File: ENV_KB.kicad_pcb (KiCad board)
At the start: 2 copper layers, 355.7 x 131.8 mm, 177 parts, among them U1 PICO_RP2040

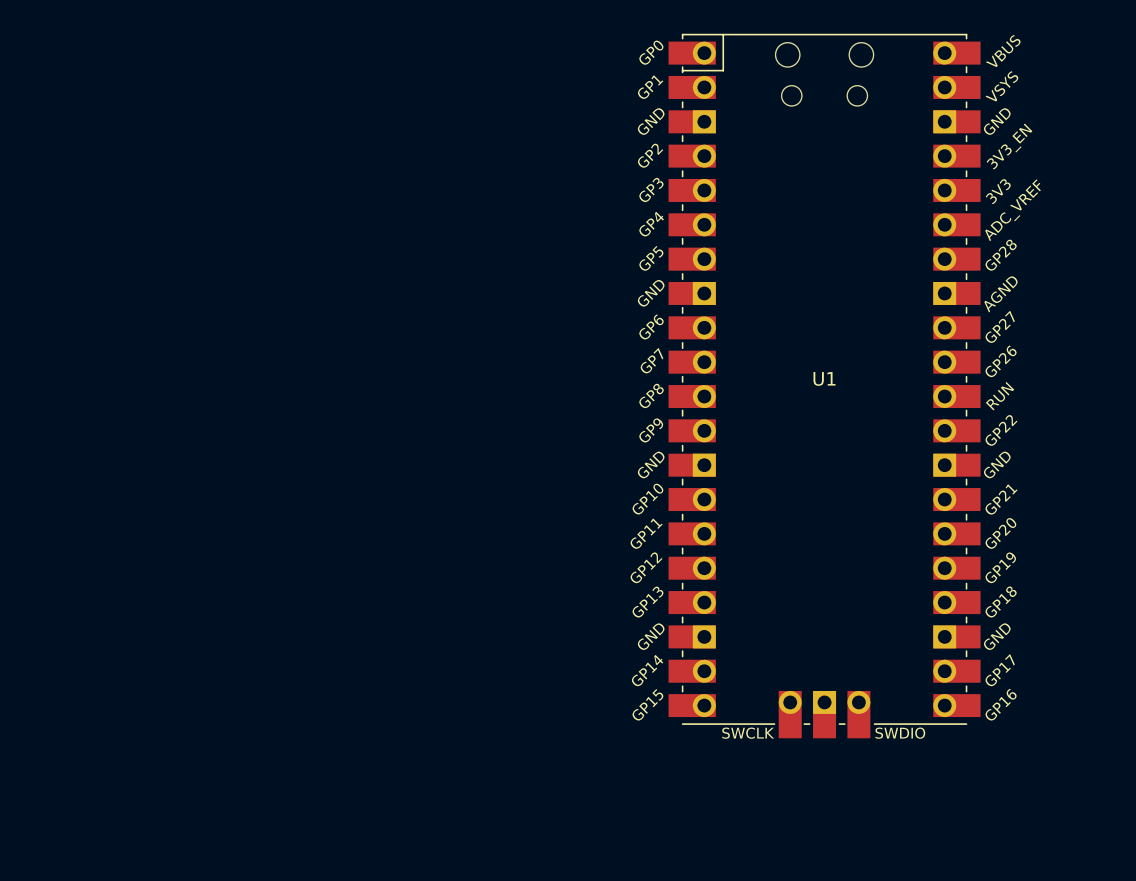
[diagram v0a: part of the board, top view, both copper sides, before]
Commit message: Updated Ratsnest
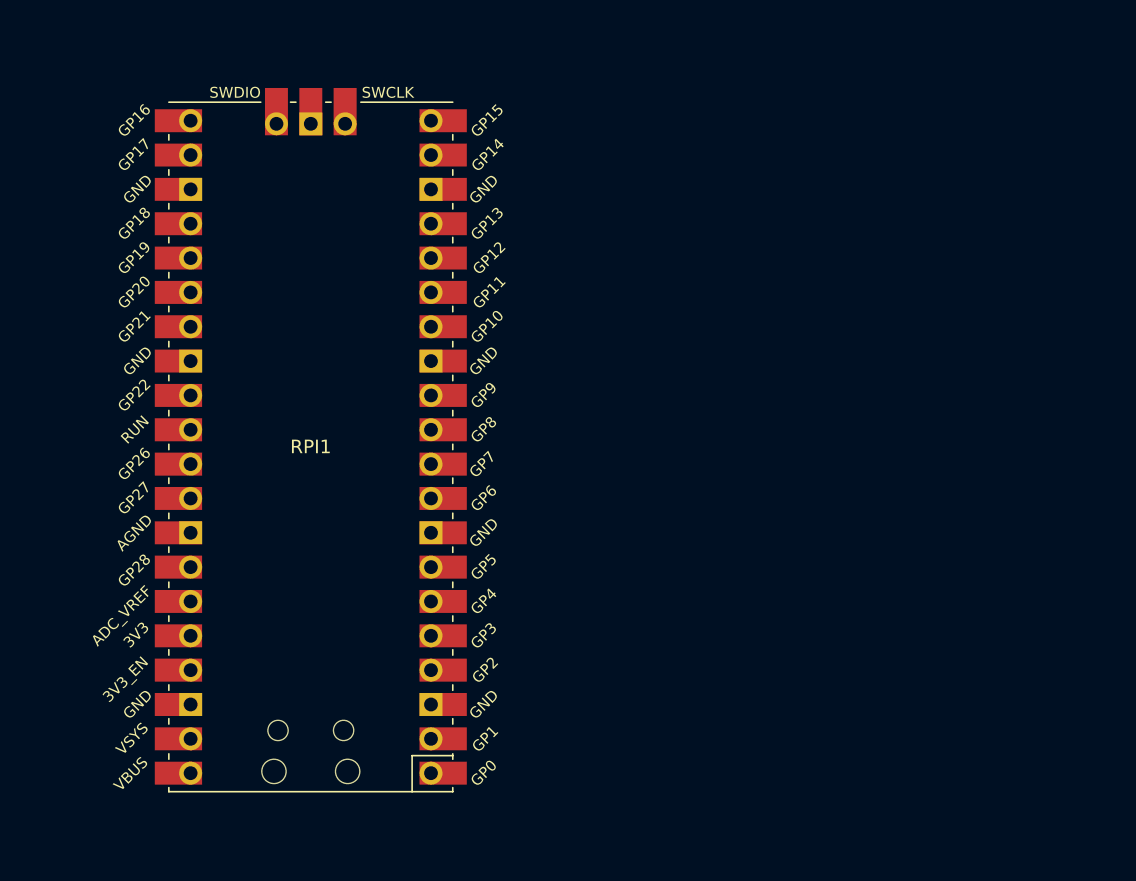
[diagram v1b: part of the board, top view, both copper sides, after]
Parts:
- removed U1: PICO_RP2040, MCU_RaspberryPi_and_Boards.pretty:RPi_Pico_SMD_TH
- added RPI1: Pico, MCU_RaspberryPi_and_Boards.pretty:RPi_Pico_SMD_TH, F.Cu at (198.0, -25.0)

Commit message: Generic Progress
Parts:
- removed RPI1: Pico, MCU_RaspberryPi_and_Boards.pretty:RPi_Pico_SMD_TH
- D_0, D_1, D_10, D_11, D_12, D_13, D_14, D_15, D_16, D_17, D_18, D_19, D_2, D_20, D_21, D_22, D_23, D_24, D_25, D_26, D_27, D_28, D_29, D_3, D_30, D_31, D_32, D_33, D_34, D_35, D_36, D_37, D_38, D_39, D_4, D_40, D_41, D_42, D_43, D_44, D_45, D_46, D_47, D_48, D_49, D_5, D_50, D_51, D_52, D_53, D_54, D_55, D_56, D_57, D_58, D_59, D_6, D_60, D_61, D_62, D_63, D_64, D_65, D_66, D_67, D_68, D_69, D_7, D_70, D_71, D_72, D_73, D_74, D_75, D_76, D_77, D_78, D_79, D_8, D_80, D_81, D_82, D_83, D_84, D_85, D_86, D_87, D_9: moved to F.Cu
- moved K_46 169.3 mm to (408.8, 204.7)
- moved K_11 169.3 mm to (392.2, 147.5)
- moved K_12 169.3 mm to (411.2, 147.5)
- moved K_13 169.3 mm to (435.0, 147.5)
- moved K_19 169.3 mm to (201.7, 176.1)
- moved K_2 169.3 mm to (201.7, 147.5)
- moved K_25 169.3 mm to (316.0, 176.1)
- moved K_30 169.3 mm to (435.0, 176.1)
- moved K_39 169.3 mm to (268.4, 195.2)
- moved K_44 169.3 mm to (363.6, 195.2)
- moved K_47 169.3 mm to (435.0, 195.2)
- moved K_5 169.3 mm to (268.4, 147.5)
- moved K_50 169.3 mm to (151.7, 214.2)
- moved K_51 169.3 mm to (177.9, 214.2)
- moved K_52 169.3 mm to (196.9, 214.2)
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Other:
- board size 355.7 x 131.8 mm -> 355.7 x 191.8 mm

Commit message: More Progress
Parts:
- removed D_0, D_1, D_10, D_11, D_12, D_13, D_14, D_15, D_16, D_17, D_18, D_19, D_2, D_20, D_21, D_22, D_23, D_24, D_25, D_26, D_27, D_28, D_29, D_3, D_30, D_31, D_32, D_33, D_34, D_35, D_36, D_37, D_38, D_39, D_4, D_40, D_41, D_42, D_43, D_44, D_45, D_46, D_47, D_48, D_49, D_5, D_50, D_51, D_52, D_53, D_54, D_55, D_56, D_57, D_58, D_59, D_6, D_60, D_61, D_62, D_63, D_64, D_65, D_66, D_67, D_68, D_69, D_70, D_71, D_72, D_73, D_74, D_75, D_76, D_77, D_78, D_79, D_80, D_81, D_82, D_83, D_84, D_85, D_86, D_87, D_9: D, Diode_THT:D_DO-35_SOD27_P7.62mm_Horizontal
- added D0: D, cftkb:D_DO-35_SOD27_P5.08mm_Horizontal, F.Cu at (143.0, 98.8)
- added D1: D, cftkb:D_DO-35_SOD27_P5.08mm_Horizontal, F.Cu at (185.1, 101.3)
- added D10: D, cftkb:D_DO-35_SOD27_P5.08mm_Horizontal, F.Cu at (396.8, 93.4)
- added D11: D, cftkb:D_DO-35_SOD27_P5.08mm_Horizontal, F.Cu at (393.2, 103.8)
- added D12: D, cftkb:D_DO-35_SOD27_P5.08mm_Horizontal, F.Cu at (393.2, 93.4)
- added D13: D, cftkb:D_DO-35_SOD27_P5.08mm_Horizontal, F.Cu at (432.1, 93.4)
- added D14: D, cftkb:D_DO-35_SOD27_P5.08mm_Horizontal, F.Cu at (467.4, 103.8)
- added D15: D, cftkb:D_DO-35_SOD27_P5.08mm_Horizontal, F.Cu at (471.0, 103.8)
- added D16: D, cftkb:D_DO-35_SOD27_P5.08mm_Horizontal, F.Cu at (146.2, 101.3)
- added D17: D, cftkb:D_DO-35_SOD27_P5.08mm_Horizontal, F.Cu at (168.9, 103.8)
- added D18: D, cftkb:D_DO-35_SOD27_P5.08mm_Horizontal, F.Cu at (181.9, 98.8)
- added D19: D, cftkb:D_DO-35_SOD27_P5.08mm_Horizontal, F.Cu at (198.1, 103.8)
- added D2: D, cftkb:D_DO-35_SOD27_P5.08mm_Horizontal, F.Cu at (201.3, 98.8)
- added D20: D, cftkb:D_DO-35_SOD27_P5.08mm_Horizontal, F.Cu at (214.2, 101.3)
- added D21: D, cftkb:D_DO-35_SOD27_P5.08mm_Horizontal, F.Cu at (230.4, 98.8)
- added D22: D, cftkb:D_DO-35_SOD27_P5.08mm_Horizontal, F.Cu at (249.9, 98.8)
- added D23: D, cftkb:D_DO-35_SOD27_P5.08mm_Horizontal, F.Cu at (262.8, 101.3)
- added D24: D, cftkb:D_DO-35_SOD27_P5.08mm_Horizontal, F.Cu at (269.3, 98.8)
- added D25: D, cftkb:D_DO-35_SOD27_P5.08mm_Horizontal, F.Cu at (285.5, 103.8)
- added D26: D, cftkb:D_DO-35_SOD27_P5.08mm_Horizontal, F.Cu at (301.7, 101.1)
- added D27: D, cftkb:D_DO-35_SOD27_P5.08mm_Horizontal, F.Cu at (403.8, 93.4)
- added D28: D, cftkb:D_DO-35_SOD27_P5.08mm_Horizontal, F.Cu at (418.0, 103.8)
- added D29: D, cftkb:D_DO-35_SOD27_P5.08mm_Horizontal, F.Cu at (428.6, 103.8)
- added D3: D, cftkb:D_DO-35_SOD27_P5.08mm_Horizontal, F.Cu at (217.5, 103.8)
- added D30: D, cftkb:D_DO-35_SOD27_P5.08mm_Horizontal, F.Cu at (456.8, 103.8)
- added D31: D, cftkb:D_DO-35_SOD27_P5.08mm_Horizontal, F.Cu at (460.4, 103.8)
- added D32: D, cftkb:D_DO-35_SOD27_P5.08mm_Horizontal, F.Cu at (463.9, 103.8)
- added D33: D, cftkb:D_DO-35_SOD27_P5.08mm_Horizontal, F.Cu at (149.5, 103.8)
- added D34: D, cftkb:D_DO-35_SOD27_P5.08mm_Horizontal, F.Cu at (172.1, 98.8)
- added D35: D, cftkb:D_DO-35_SOD27_P5.08mm_Horizontal, F.Cu at (188.3, 103.8)
- added D36: D, cftkb:D_DO-35_SOD27_P5.08mm_Horizontal, F.Cu at (204.5, 101.3)
- added D37: D, cftkb:D_DO-35_SOD27_P5.08mm_Horizontal, F.Cu at (220.7, 98.8)
- added D38: D, cftkb:D_DO-35_SOD27_P5.08mm_Horizontal, F.Cu at (236.9, 103.8)
- added D39: D, cftkb:D_DO-35_SOD27_P5.08mm_Horizontal, F.Cu at (253.1, 101.3)
- added D4: D, cftkb:D_DO-35_SOD27_P5.08mm_Horizontal, F.Cu at (233.7, 101.3)
- added D40: D, cftkb:D_DO-35_SOD27_P5.08mm_Horizontal, F.Cu at (272.6, 101.3)
- added D41: D, cftkb:D_DO-35_SOD27_P5.08mm_Horizontal, F.Cu at (282.3, 101.1)
- added D42: D, cftkb:D_DO-35_SOD27_P5.08mm_Horizontal, F.Cu at (288.8, 98.8)
- added D43: D, cftkb:D_DO-35_SOD27_P5.08mm_Horizontal, F.Cu at (403.8, 103.8)
- added D44: D, cftkb:D_DO-35_SOD27_P5.08mm_Horizontal, F.Cu at (418.0, 93.4)
- added D45: D, cftkb:D_DO-35_SOD27_P5.08mm_Horizontal, F.Cu at (421.5, 93.4)
- added D46: D, cftkb:D_DO-35_SOD27_P5.08mm_Horizontal, F.Cu at (428.6, 93.4)
- added D47: D, cftkb:D_DO-35_SOD27_P5.08mm_Horizontal, F.Cu at (446.2, 103.8)
- added D48: D, cftkb:D_DO-35_SOD27_P5.08mm_Horizontal, F.Cu at (449.8, 103.8)
- added D49: D, cftkb:D_DO-35_SOD27_P5.08mm_Horizontal, F.Cu at (453.3, 103.8)
- added D5: D, cftkb:D_DO-35_SOD27_P5.08mm_Horizontal, F.Cu at (266.1, 103.8)
- added D50: D, cftkb:D_DO-35_SOD27_P5.08mm_Horizontal, F.Cu at (152.7, 98.8)
- added D51: D, CFTKB Bits:D_DO-35_SOD27_P5.08mm_Horizontal, F.Cu at (308.0, 101.1)
- added D52: D, cftkb:D_DO-35_SOD27_P5.08mm_Horizontal, F.Cu at (175.4, 101.3)
- added D53: D, cftkb:D_DO-35_SOD27_P5.08mm_Horizontal, F.Cu at (191.6, 98.8)
- added D54: D, cftkb:D_DO-35_SOD27_P5.08mm_Horizontal, F.Cu at (207.8, 103.8)
- added D55: D, cftkb:D_DO-35_SOD27_P5.08mm_Horizontal, F.Cu at (224.0, 101.3)
- added D56: D, cftkb:D_DO-35_SOD27_P5.08mm_Horizontal, F.Cu at (240.2, 98.8)
- added D57: D, cftkb:D_DO-35_SOD27_P5.08mm_Horizontal, F.Cu at (256.4, 103.8)
- added D58: D, cftkb:D_DO-35_SOD27_P5.08mm_Horizontal, F.Cu at (275.8, 103.8)
- added D59: D, cftkb:D_DO-35_SOD27_P5.08mm_Horizontal, F.Cu at (292.0, 101.1)
- added D6: D, cftkb:D_DO-35_SOD27_P5.08mm_Horizontal, F.Cu at (298.5, 98.8)
- added D60: D, cftkb:D_DO-35_SOD27_P5.08mm_Horizontal, F.Cu at (305.0, 103.8)
- added D61: D, cftkb:D_DO-35_SOD27_P5.08mm_Horizontal, F.Cu at (407.4, 93.4)
- added D62: D, cftkb:D_DO-35_SOD27_P5.08mm_Horizontal, F.Cu at (414.4, 103.8)
- added D63: D, cftkb:D_DO-35_SOD27_P5.08mm_Horizontal, F.Cu at (425.0, 103.8)
- added D64: D, cftkb:D_DO-35_SOD27_P5.08mm_Horizontal, F.Cu at (155.9, 101.3)
- added D65: D, cftkb:D_DO-35_SOD27_P5.08mm_Horizontal, F.Cu at (178.6, 103.8)
- added D66: D, cftkb:D_DO-35_SOD27_P5.08mm_Horizontal, F.Cu at (194.8, 101.3)
- added D67: D, cftkb:D_DO-35_SOD27_P5.08mm_Horizontal, F.Cu at (211.0, 98.8)
- added D68: D, cftkb:D_DO-35_SOD27_P5.08mm_Horizontal, F.Cu at (227.2, 103.8)
- added D69: D, cftkb:D_DO-35_SOD27_P5.08mm_Horizontal, F.Cu at (243.4, 101.3)
- added D70: D, cftkb:D_DO-35_SOD27_P5.08mm_Horizontal, F.Cu at (259.6, 98.8)
- added D71: D, cftkb:D_DO-35_SOD27_P5.08mm_Horizontal, F.Cu at (279.0, 98.8)
- added D72: D, cftkb:D_DO-35_SOD27_P5.08mm_Horizontal, F.Cu at (295.2, 103.8)
- added D73: D, cftkb:D_DO-35_SOD27_P5.08mm_Horizontal, F.Cu at (407.4, 103.8)
- added D74: D, cftkb:D_DO-35_SOD27_P5.08mm_Horizontal, F.Cu at (414.4, 93.4)
- added D75: D, cftkb:D_DO-35_SOD27_P5.08mm_Horizontal, F.Cu at (425.0, 93.4)
- added D76: D, cftkb:D_DO-35_SOD27_P5.08mm_Horizontal, F.Cu at (442.7, 103.8)
- added D77: D, cftkb:D_DO-35_SOD27_P5.08mm_Horizontal, F.Cu at (159.2, 103.8)
- added D78: D, CFTKB Bits:D_DO-35_SOD27_P5.08mm_Horizontal, F.Cu at (385.5, 66.0)
- added D79: D, cftkb:D_DO-35_SOD27_P5.08mm_Horizontal, F.Cu at (162.4, 98.8)
- added D80: D, CFTKB Bits:D_DO-35_SOD27_P5.08mm_Horizontal, F.Cu at (394.2, 62.5)
- added D81: D, cftkb:D_DO-35_SOD27_P5.08mm_Horizontal, F.Cu at (165.7, 101.3)
- added D82: D, CFTKB Bits:D_DO-35_SOD27_P5.08mm_Horizontal, F.Cu at (385.5, 69.6)
- added D83: D, cftkb:D_DO-35_SOD27_P5.08mm_Horizontal, F.Cu at (246.6, 103.8)
- added D84: D, CFTKB Bits:D_DO-35_SOD27_P5.08mm_Horizontal, F.Cu at (394.2, 66.0)
- added D85: D, cftkb:D_DO-35_SOD27_P5.08mm_Horizontal, F.Cu at (410.9, 93.4)
- added D86: D, cftkb:D_DO-35_SOD27_P5.08mm_Horizontal, F.Cu at (410.9, 103.8)
- added D87: D, CFTKB Bits:D_DO-35_SOD27_P5.08mm_Horizontal, F.Cu at (385.5, 73.2)
- added D88: D_Small, cftkb:D_DO-35_SOD27_P5.08mm_Horizontal, F.Cu at (421.5, 103.8)
- added D9: D, cftkb:D_DO-35_SOD27_P5.08mm_Horizontal, F.Cu at (396.8, 103.8)
- added D90: D_Small, cftkb:D_DO-35_SOD27_P5.08mm_Horizontal, F.Cu at (432.1, 103.8)
- added D92: D_Small, cftkb:D_DO-35_SOD27_P5.08mm_Horizontal, F.Cu at (435.6, 93.4)
- added D93: D_Small, cftkb:D_DO-35_SOD27_P5.08mm_Horizontal, F.Cu at (435.6, 103.8)
- added D94: D_Small, cftkb:D_DO-35_SOD27_P5.08mm_Horizontal, F.Cu at (439.2, 103.8)
- D_7, D_8: footprint Diode_THT:D_DO-35_SOD27_P7.62mm_Horizontal -> CFTKB Bits:D_DO-35_SOD27_P5.08mm_Horizontal
- K_80: footprint MX_Only:MXOnly-6.25U-NoLED -> MX_only:MXOnly-6.25U-ReversedStabilizers-NoLED
- moved D_7 92.6 mm to (400.7, 103.8)
- moved D_8 76.3 mm to (400.2, 93.4)
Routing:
- net row0: track 0.00 -> 376.8 mm, vias 0 -> 4
- net row2: track 0.00 -> 277.7 mm, vias 0 -> 4
- net row3: track 0.00 -> 273.3 mm, vias 0 -> 1
- net row5: track 0.00 -> 258.1 mm, vias 0 -> 5
- net row4: track 0.00 -> 182.8 mm, vias 0 -> 1
- net row6: track 0.00 -> 162.8 mm
- net (no net): track 0.00 -> 143.7 mm, vias 0 -> 3
- net col0: track 0.00 -> 135.4 mm
- net col3: track 0.00 -> 130.9 mm
- net col14: track 0.00 -> 127.1 mm
- net col13: track 0.00 -> 125.8 mm
- net col10: track 0.00 -> 124.6 mm
- net col6: track 0.00 -> 122.1 mm
- net col11: track 0.00 -> 121.7 mm
- net col1: track 0.00 -> 117.9 mm
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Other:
- board size 355.7 x 191.8 mm -> 355.7 x 173.2 mm

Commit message: MORE TRACES and DIODE STUFF!
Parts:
- moved D80 262.1 mm to (138.7, 121.0), turned to 270 degrees
- moved D78 249.4 mm to (141.7, 118.5), turned to 270 degrees
- moved D87 70.1 mm to (444.8, 110.6), turned to 270 degrees
- moved D84 64.8 mm to (441.2, 110.6), turned to 270 degrees
- moved D82 51.7 mm to (391.6, 121.0), turned to 270 degrees
- moved D0 17.3 mm to (145.0, 116.0)
- moved D1 17.3 mm to (187.1, 118.5)
- moved D10 17.3 mm to (398.8, 110.6)
- moved D11 17.3 mm to (395.2, 121.0)
- moved D12 17.3 mm to (395.2, 110.6)
- moved D13 17.3 mm to (434.1, 110.6)
- moved D14 17.3 mm to (469.4, 121.0)
- moved D15 17.3 mm to (473.0, 121.0)
- moved D16 17.3 mm to (148.2, 118.5)
- moved D17 17.3 mm to (170.9, 121.0)
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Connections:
- D88 pad 1: (no net) -> row6
- D90 pad 1: (no net) -> row6
- D92 pad 1: (no net) -> row6
- D93 pad 1: (no net) -> row6
- D94 pad 1: (no net) -> row6
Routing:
- net (no net): track 143.7 -> 24.8 mm, vias 3 -> 0
- net row6: track 162.8 -> 268.2 mm, vias 0 -> 2
- net row4: track 182.8 -> 204.1 mm, vias 1 -> 2
- net row5: track 258.1 -> 269.4 mm
- net Net-(D75-Pad2): track 2.07 -> 12.3 mm
- net Net-(D45-Pad2): track 7.67 -> 14.4 mm
- net row0: track 376.8 -> 376.7 mm, vias 4 -> 5

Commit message: Adjusted Diodes, Traces + added logo
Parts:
- removed D88, D90, D92, D93, D94: D_Small, cftkb:D_DO-35_SOD27_P5.08mm_Horizontal
- added G***: LOGO, EM_Logo:PersonalLogo, F.Cu at (455.9, 214.8)
- added RPI1: Pico, MCU_RaspberryPi_and_Boards.pretty:RPi_Pico_SMD_TH, F.Cu at (362.1, 121.5)
- D0, D1, D10, D11, D12, D13, D14, D15, D16, D17, D18, D19, D2, D20, D21, D22, D23, D24, D25, D26, D27, D28, D29, D3, D30, D31, D32, D33, D34, D35, D36, D37, D38, D39, D4, D40, D41, D42, D43, D44, D45, D46, D47, D48, D49, D5, D50, D52, D53, D54, D55, D56, D57, D58, D59, D6, D60, D61, D62, D63, D64, D65, D66, D67, D68, D69, D70, D71, D72, D73, D74, D75, D76, D77, D79, D81, D83, D85, D86, D9: footprint cftkb:D_DO-35_SOD27_P5.08mm_Horizontal -> CFTKB Bits:D_DO-35_SOD27_P5.08mm_Horizontal
- K_0, K_1, K_10, K_11, K_12, K_13, K_14, K_15, K_16, K_17, K_18, K_19, K_2, K_20, K_21, K_22, K_23, K_24, K_25, K_26, K_27, K_28, K_3, K_30, K_31, K_32, K_34, K_35, K_36, K_37, K_38, K_39, K_4, K_40, K_41, K_42, K_43, K_44, K_45, K_47, K_48, K_49, K_5, K_51, K_52, K_53, K_54, K_55, K_56, K_57, K_58, K_59, K_6, K_60, K_61, K_62, K_64, K_65, K_66, K_67, K_68, K_69, K_7, K_70, K_71, K_72, K_73, K_74, K_76, K_8, K_85, K_86, K_87, K_9: footprint MX_Only:MXOnly-1U-NoLED -> MX_only:MXOnly-1U-NoLED
- K_29: footprint MX_Only:MXOnly-2U-NoLED -> MX_only:MXOnly-2U-NoLED
- K_33: footprint MX_Only:MXOnly-1.5U-NoLED -> MX_only:MXOnly-1.5U-NoLED
- K_46: footprint MX_Only:MXOnly-ISO-ROTATED-ReversedStabilizers-NoLED -> MX_only:MXOnly-ISO-ROTATED-ReversedStabilizers-NoLED
- K_50: footprint MX_Only:MXOnly-1.75U-NoLED -> MX_only:MXOnly-1.75U-NoLED
- K_63, K_77, K_78, K_79, K_81, K_82, K_83, K_84: footprint MX_Only:MXOnly-1.25U-NoLED -> MX_only:MXOnly-1.25U-NoLED
- K_75: footprint MX_Only:MXOnly-2.75U-NoLED -> MX_only:MXOnly-2.75U-NoLED
- moved D82 42.9 mm to (434.5, 121.0)
- moved D87 23.6 mm to (423.6, 121.0)
- moved D84 10.8 mm to (438.1, 121.0)
- moved D0 4.13 mm to (141.7, 118.5)
- moved D78 3.98 mm to (144.9, 116.1)
- moved D11 3.97 mm to (399.2, 121.0)
- moved D9 2.96 mm to (395.8, 121.0)
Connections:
- D61 pad 1: row4 -> row5
- D62 pad 1: row4 -> row5
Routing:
- net col0: track 135.4 -> 313.7 mm
- net col1: track 117.9 -> 285.5 mm
- net col2: track 106.0 -> 251.1 mm
- net col3: track 130.9 -> 259.4 mm
- net col4: track 106.8 -> 215.3 mm
- net col5: track 105.4 -> 193.7 mm
- net col6: track 122.1 -> 199.1 mm
- net col17: track 115.0 -> 190.1 mm
- net col7: track 111.0 -> 171.9 mm
- net col16: track 113.8 -> 170.3 mm
- net col8: track 104.8 -> 153.7 mm
- net row5: track 269.4 -> 314.0 mm, vias 5 -> 6
- net col15: track 112.5 -> 150.1 mm
- net col9: track 101.9 -> 134.5 mm
- net row4: track 204.1 -> 175.6 mm, vias 2 -> 1
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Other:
- board size 355.7 x 173.2 mm -> 355.7 x 160.8 mm
- rule pad_to_mask_clearance: 0 -> 0.051

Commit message: Undid diode mess / Done rest of  Switch Traces
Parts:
- removed D0, D1, D10, D11, D12, D13, D14, D15, D16, D17, D18, D19, D2, D20, D21, D22, D23, D24, D25, D26, D27, D28, D29, D3, D30, D31, D32, D33, D34, D35, D36, D37, D38, D39, D4, D40, D41, D42, D43, D44, D45, D46, D47, D48, D49, D5, D50, D51, D52, D53, D54, D55, D56, D57, D58, D59, D6, D60, D61, D62, D63, D64, D65, D66, D67, D68, D69, D70, D71, D72, D73, D74, D75, D76, D77, D78, D79, D80, D81, D82, D83, D84, D85, D86, D87, D9, D_7, D_8: D, CFTKB Bits:D_DO-35_SOD27_P5.08mm_Horizontal
- removed G***: LOGO, EM_Logo:PersonalLogo
- removed RPI1: Pico, MCU_RaspberryPi_and_Boards.pretty:RPi_Pico_SMD_TH
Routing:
- net row0: track 381.0 -> 0.00 mm, vias 3 -> 0
- net row5: track 314.0 -> 0.00 mm, vias 6 -> 0
- net row3: track 284.3 -> 0.00 mm, vias 3 -> 0
- net row2: track 283.1 -> 0.00 mm, vias 4 -> 0
- net row6: track 275.4 -> 0.00 mm, vias 2 -> 0
- net row4: track 175.6 -> 0.00 mm, vias 1 -> 0
- net Net-(D82-Pad2): track 0.00 -> 125.6 mm
- net Net-(D80-Pad2): track 0.00 -> 124.1 mm
- net Net-(D65-Pad2): track 3.63 -> 126.5 mm
- net Net-(D84-Pad2): track 0.00 -> 117.5 mm
- net Net-(D77-Pad2): track 8.00 -> 122.8 mm
- net Net-(D86-Pad2): track 0.00 -> 114.2 mm
- net Net-(D73-Pad2): track 0.00 -> 114.0 mm
- net Net-(D87-Pad2): track 0.00 -> 113.8 mm
- net Net-(D78-Pad2): track 12.6 -> 125.4 mm
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
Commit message: Replaced Diodes in horizontal stack
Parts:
- added D0: D, CFTKB Bits:D_DO-35_SOD27_P5.08mm_Horizontal, F.Cu at (148.5, 132.0)
- added D1: D, CFTKB Bits:D_DO-35_SOD27_P5.08mm_Horizontal, F.Cu at (179.0, 132.0)
- added D10: D, CFTKB Bits:D_DO-35_SOD27_P5.08mm_Horizontal, F.Cu at (360.0, 132.0)
- added D11: D, CFTKB Bits:D_DO-35_SOD27_P5.08mm_Horizontal, F.Cu at (381.0, 132.0)
- added D12: D, CFTKB Bits:D_DO-35_SOD27_P5.08mm_Horizontal, F.Cu at (398.5, 132.0)
- added D13: D, CFTKB Bits:D_DO-35_SOD27_P5.08mm_Horizontal, F.Cu at (419.5, 132.0)
- added D14: D, CFTKB Bits:D_DO-35_SOD27_P5.08mm_Horizontal, F.Cu at (435.0, 132.0)
- added D15: D, CFTKB Bits:D_DO-35_SOD27_P5.08mm_Horizontal, F.Cu at (463.0, 132.0)
- added D16: D, CFTKB Bits:D_DO-35_SOD27_P5.08mm_Horizontal, F.Cu at (148.5, 128.0)
- added D17: D, CFTKB Bits:D_DO-35_SOD27_P5.08mm_Horizontal, F.Cu at (162.0, 128.0)
- added D18: D, CFTKB Bits:D_DO-35_SOD27_P5.08mm_Horizontal, F.Cu at (179.0, 128.0)
- added D19: D, CFTKB Bits:D_DO-35_SOD27_P5.08mm_Horizontal, F.Cu at (195.5, 128.0)
- added D2: D, CFTKB Bits:D_DO-35_SOD27_P5.08mm_Horizontal, F.Cu at (195.5, 132.0)
- added D20: D, CFTKB Bits:D_DO-35_SOD27_P5.08mm_Horizontal, F.Cu at (212.5, 128.0)
- added D21: D, CFTKB Bits:D_DO-35_SOD27_P5.08mm_Horizontal, F.Cu at (229.5, 128.0)
- added D22: D, CFTKB Bits:D_DO-35_SOD27_P5.08mm_Horizontal, F.Cu at (246.0, 128.0)
- added D23: D, CFTKB Bits:D_DO-35_SOD27_P5.08mm_Horizontal, F.Cu at (260.0, 128.0)
- added D24: D, CFTKB Bits:D_DO-35_SOD27_P5.08mm_Horizontal, F.Cu at (281.5, 128.0)
- added D25: D, CFTKB Bits:D_DO-35_SOD27_P5.08mm_Horizontal, F.Cu at (300.5, 128.0)
- added D26: D, CFTKB Bits:D_DO-35_SOD27_P5.08mm_Horizontal, F.Cu at (315.5, 128.0)
- added D27: D, CFTKB Bits:D_DO-35_SOD27_P5.08mm_Horizontal, F.Cu at (340.0, 128.0)
- added D28: D, CFTKB Bits:D_DO-35_SOD27_P5.08mm_Horizontal, F.Cu at (360.0, 128.0)
- added D29: D, CFTKB Bits:D_DO-35_SOD27_P5.08mm_Horizontal, F.Cu at (398.5, 128.0)
- added D3: D, CFTKB Bits:D_DO-35_SOD27_P5.08mm_Horizontal, F.Cu at (212.5, 132.0)
- added D30: D, CFTKB Bits:D_DO-35_SOD27_P5.08mm_Horizontal, F.Cu at (419.5, 128.0)
- added D31: D, CFTKB Bits:D_DO-35_SOD27_P5.08mm_Horizontal, F.Cu at (435.0, 128.0)
- added D32: D, CFTKB Bits:D_DO-35_SOD27_P5.08mm_Horizontal, F.Cu at (463.0, 128.0)
- added D33: D, CFTKB Bits:D_DO-35_SOD27_P5.08mm_Horizontal, F.Cu at (148.5, 124.0)
- added D34: D, CFTKB Bits:D_DO-35_SOD27_P5.08mm_Horizontal, F.Cu at (179.0, 124.0)
- added D35: D, CFTKB Bits:D_DO-35_SOD27_P5.08mm_Horizontal, F.Cu at (195.5, 124.0)
- added D36: D, CFTKB Bits:D_DO-35_SOD27_P5.08mm_Horizontal, F.Cu at (212.5, 124.0)
- added D37: D, CFTKB Bits:D_DO-35_SOD27_P5.08mm_Horizontal, F.Cu at (229.5, 124.0)
- added D38: D, CFTKB Bits:D_DO-35_SOD27_P5.08mm_Horizontal, F.Cu at (246.0, 124.0)
- added D39: D, CFTKB Bits:D_DO-35_SOD27_P5.08mm_Horizontal, F.Cu at (260.0, 124.0)
- added D4: D, CFTKB Bits:D_DO-35_SOD27_P5.08mm_Horizontal, F.Cu at (229.5, 132.0)
- added D40: D, CFTKB Bits:D_DO-35_SOD27_P5.08mm_Horizontal, F.Cu at (281.5, 124.0)
- added D41: D, CFTKB Bits:D_DO-35_SOD27_P5.08mm_Horizontal, F.Cu at (300.5, 124.0)
- added D42: D, CFTKB Bits:D_DO-35_SOD27_P5.08mm_Horizontal, F.Cu at (315.5, 124.0)
- added D43: D, CFTKB Bits:D_DO-35_SOD27_P5.08mm_Horizontal, F.Cu at (340.0, 124.0)
- added D44: D, CFTKB Bits:D_DO-35_SOD27_P5.08mm_Horizontal, F.Cu at (360.0, 124.0)
- added D45: D, CFTKB Bits:D_DO-35_SOD27_P5.08mm_Horizontal, F.Cu at (381.0, 124.0)
- added D46: D, CFTKB Bits:D_DO-35_SOD27_P5.08mm_Horizontal, F.Cu at (398.5, 124.0)
- added D47: D, CFTKB Bits:D_DO-35_SOD27_P5.08mm_Horizontal, F.Cu at (419.5, 124.0)
- added D48: D, CFTKB Bits:D_DO-35_SOD27_P5.08mm_Horizontal, F.Cu at (435.0, 124.0)
- added D49: D, CFTKB Bits:D_DO-35_SOD27_P5.08mm_Horizontal, F.Cu at (463.0, 124.0)
- added D5: D, CFTKB Bits:D_DO-35_SOD27_P5.08mm_Horizontal, F.Cu at (260.0, 132.0)
- added D50: D, CFTKB Bits:D_DO-35_SOD27_P5.08mm_Horizontal, F.Cu at (148.5, 120.0)
- added D51: D, CFTKB Bits:D_DO-35_SOD27_P5.08mm_Horizontal, F.Cu at (179.0, 120.0)
- added D52: D, CFTKB Bits:D_DO-35_SOD27_P5.08mm_Horizontal, F.Cu at (195.5, 120.0)
- added D53: D, CFTKB Bits:D_DO-35_SOD27_P5.08mm_Horizontal, F.Cu at (212.5, 120.0)
- added D54: D, CFTKB Bits:D_DO-35_SOD27_P5.08mm_Horizontal, F.Cu at (229.5, 120.0)
- added D55: D, CFTKB Bits:D_DO-35_SOD27_P5.08mm_Horizontal, F.Cu at (246.0, 120.0)
- added D56: D, CFTKB Bits:D_DO-35_SOD27_P5.08mm_Horizontal, F.Cu at (260.0, 120.0)
- added D57: D, CFTKB Bits:D_DO-35_SOD27_P5.08mm_Horizontal, F.Cu at (281.5, 120.0)
- added D58: D, CFTKB Bits:D_DO-35_SOD27_P5.08mm_Horizontal, F.Cu at (300.5, 120.0)
- added D59: D, CFTKB Bits:D_DO-35_SOD27_P5.08mm_Horizontal, F.Cu at (315.5, 120.0)
- added D6: D, CFTKB Bits:D_DO-35_SOD27_P5.08mm_Horizontal, F.Cu at (281.5, 132.0)
- added D60: D, CFTKB Bits:D_DO-35_SOD27_P5.08mm_Horizontal, F.Cu at (340.0, 120.0)
- added D61: D, CFTKB Bits:D_DO-35_SOD27_P5.08mm_Horizontal, F.Cu at (360.0, 120.0)
- added D62: D, CFTKB Bits:D_DO-35_SOD27_P5.08mm_Horizontal, F.Cu at (381.0, 120.0)
- added D63: D, CFTKB Bits:D_DO-35_SOD27_P5.08mm_Horizontal, F.Cu at (148.5, 116.0)
- added D64: D, CFTKB Bits:D_DO-35_SOD27_P5.08mm_Horizontal, F.Cu at (162.0, 116.0)
- added D65: D, CFTKB Bits:D_DO-35_SOD27_P5.08mm_Horizontal, F.Cu at (179.0, 116.0)
- added D66: D, CFTKB Bits:D_DO-35_SOD27_P5.08mm_Horizontal, F.Cu at (195.5, 116.0)
- added D67: D, CFTKB Bits:D_DO-35_SOD27_P5.08mm_Horizontal, F.Cu at (212.5, 116.0)
- added D68: D, CFTKB Bits:D_DO-35_SOD27_P5.08mm_Horizontal, F.Cu at (229.5, 116.0)
- added D69: D, CFTKB Bits:D_DO-35_SOD27_P5.08mm_Horizontal, F.Cu at (246.0, 116.0)
- added D70: D, CFTKB Bits:D_DO-35_SOD27_P5.08mm_Horizontal, F.Cu at (260.0, 116.0)
- added D71: D, CFTKB Bits:D_DO-35_SOD27_P5.08mm_Horizontal, F.Cu at (281.5, 116.0)
- added D72: D, CFTKB Bits:D_DO-35_SOD27_P5.08mm_Horizontal, F.Cu at (300.5, 116.0)
- added D73: D, CFTKB Bits:D_DO-35_SOD27_P5.08mm_Horizontal, F.Cu at (315.5, 116.0)
- added D74: D, CFTKB Bits:D_DO-35_SOD27_P5.08mm_Horizontal, F.Cu at (340.0, 116.0)
- added D75: D, CFTKB Bits:D_DO-35_SOD27_P5.08mm_Horizontal, F.Cu at (381.0, 116.0)
- added D76: D, CFTKB Bits:D_DO-35_SOD27_P5.08mm_Horizontal, F.Cu at (435.0, 116.0)
- added D77: D, CFTKB Bits:D_DO-35_SOD27_P5.08mm_Horizontal, F.Cu at (148.5, 112.0)
- added D78: D, CFTKB Bits:D_DO-35_SOD27_P5.08mm_Horizontal, F.Cu at (162.0, 112.0)
- added D79: D, CFTKB Bits:D_DO-35_SOD27_P5.08mm_Horizontal, F.Cu at (195.5, 112.0)
- added D80: D, CFTKB Bits:D_DO-35_SOD27_P5.08mm_Horizontal, F.Cu at (246.0, 112.0)
- added D81: D, CFTKB Bits:D_DO-35_SOD27_P5.08mm_Horizontal, F.Cu at (315.5, 112.0)
- added D82: D, CFTKB Bits:D_DO-35_SOD27_P5.08mm_Horizontal, F.Cu at (340.0, 112.0)
- added D83: D, CFTKB Bits:D_DO-35_SOD27_P5.08mm_Horizontal, F.Cu at (381.0, 112.0)
- added D84: D, CFTKB Bits:D_DO-35_SOD27_P5.08mm_Horizontal, F.Cu at (398.5, 112.0)
- added D85: D, CFTKB Bits:D_DO-35_SOD27_P5.08mm_Horizontal, F.Cu at (419.5, 112.0)
- added D86: D, CFTKB Bits:D_DO-35_SOD27_P5.08mm_Horizontal, F.Cu at (435.0, 112.0)
- added D87: D, CFTKB Bits:D_DO-35_SOD27_P5.08mm_Horizontal, F.Cu at (463.0, 112.0)
- added D9: D, CFTKB Bits:D_DO-35_SOD27_P5.08mm_Horizontal, F.Cu at (340.0, 132.0)
- added D_7: D, CFTKB Bits:D_DO-35_SOD27_P5.08mm_Horizontal, F.Cu at (300.5, 132.0)
- added D_8: D, CFTKB Bits:D_DO-35_SOD27_P5.08mm_Horizontal, F.Cu at (315.5, 132.0)
- added RPI1: Pico, MCU_RaspberryPi_and_Boards.pretty:RPi_Pico_SMD_TH, F.Cu at (317.4, 59.1)
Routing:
- net Net-(D78-Pad2): track 125.4 -> 118.3 mm
- net Net-(D63-Pad2): track 108.8 -> 101.8 mm
- net Net-(D64-Pad2): track 111.3 -> 104.4 mm
- net Net-(D17-Pad2): track 47.6 -> 41.6 mm
- net Net-(D33-Pad2): track 60.1 -> 64.4 mm
- net Net-(D77-Pad2): track 122.8 -> 118.6 mm
- net Net-(D16-Pad2): track 42.6 -> 39.1 mm
- net Net-(D50-Pad2): track 82.6 -> 85.5 mm
- net Net-(D0-Pad2): track 14.0 -> 12.1 mm
